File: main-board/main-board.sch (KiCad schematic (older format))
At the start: 57 parts, among them J1 C10418, J2 FH12-24S-0.5SH(55), J3 TF-01A, Q1 Q_NPN_BCE, Q2 Q_NPN_BCE, SW1 SW_DIP_x01, U1 ESP-32s, U2 HT7333-A, U3 CH340E, U4 DW06D, U5 IPS6404L-SQ-SPN, U6 SX1308, U7 RT9011-CMGJ6, U8 SN74LVC125ADBR

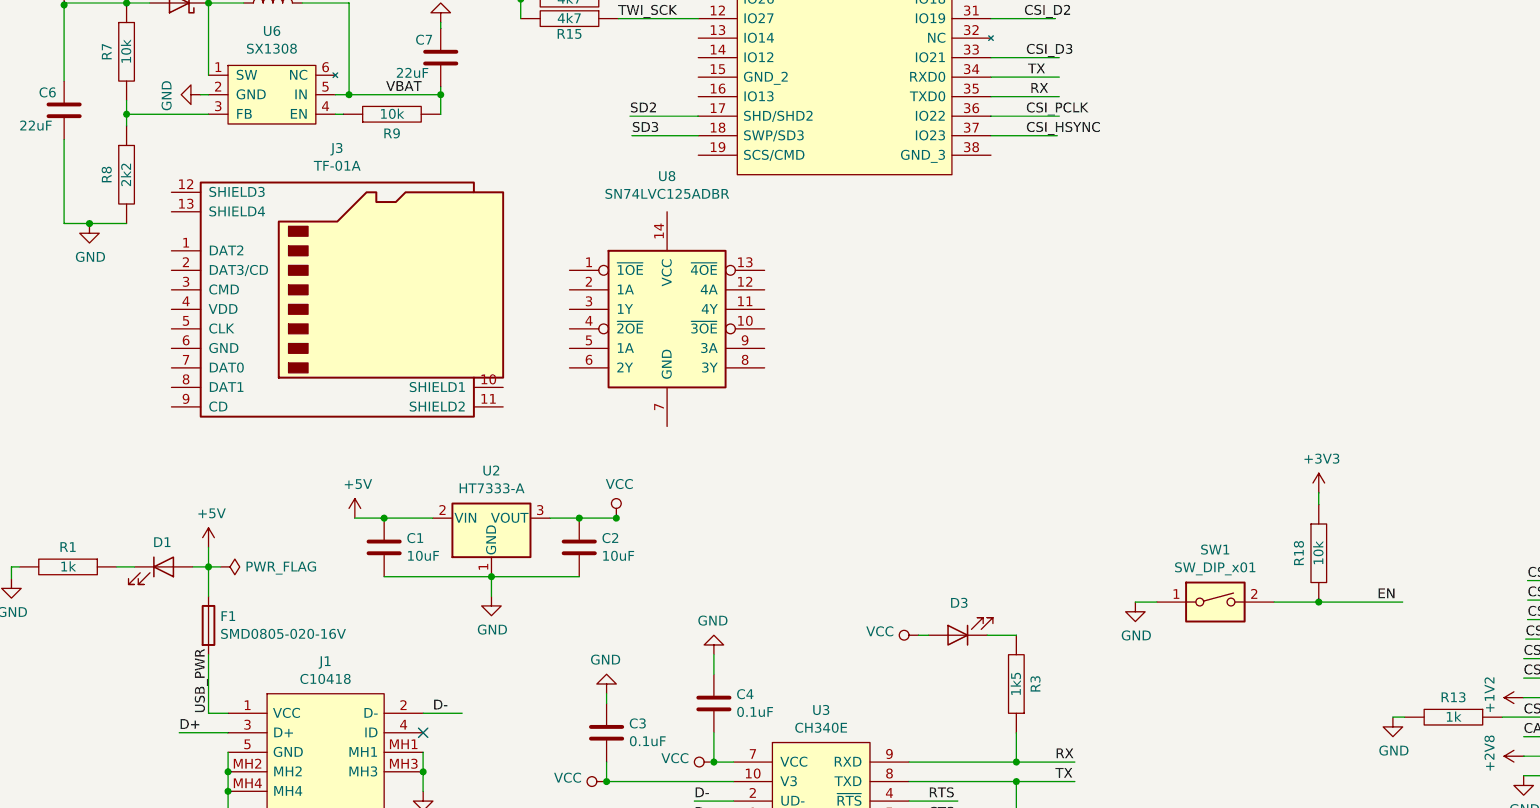
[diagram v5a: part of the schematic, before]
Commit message: SD passive and wires
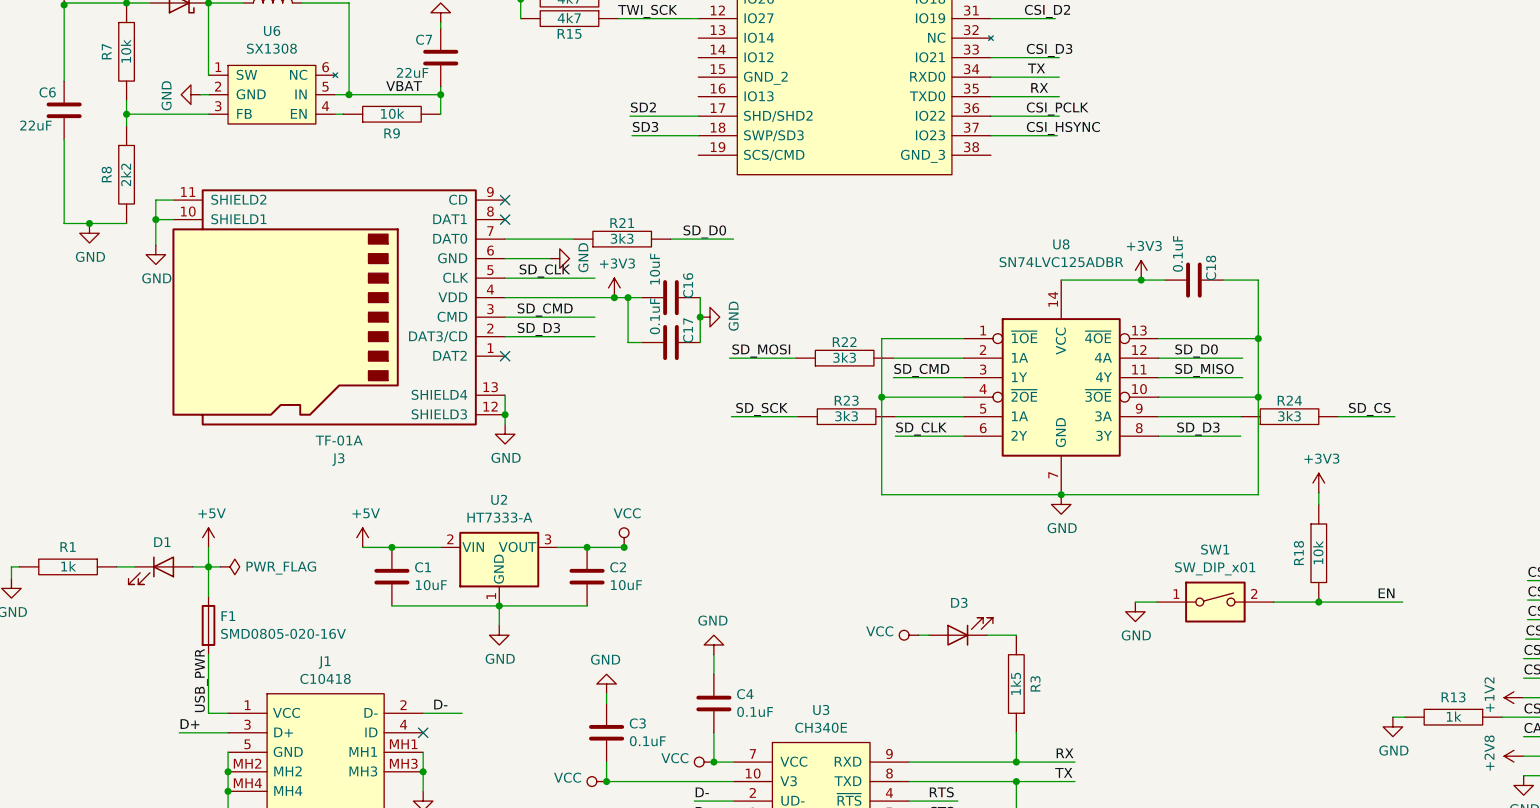
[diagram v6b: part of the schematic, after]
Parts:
- added C16: 10uF, Capacitor_SMD:C_0805_2012Metric_Pad1.15x1.40mm_HandSolder, symbol Device:C
- added C17, C18: 0.1uF, Capacitor_SMD:C_0805_2012Metric_Pad1.15x1.40mm_HandSolder, symbol Device:C
- added R21, R22, R23, R24: 3k3, Resistor_SMD:R_0805_2012Metric_Pad1.15x1.40mm_HandSolder, symbol pspice:R
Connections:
- net labels added: SD_CLK, SD_CMD, SD_CS, SD_D0, SD_D3, SD_MISO, SD_MOSI, SD_SCK
- wire segments 201 -> 245
- no-connect marks 5 -> 8
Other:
- moved on the sheet: C1, C2, J3, U2, U8

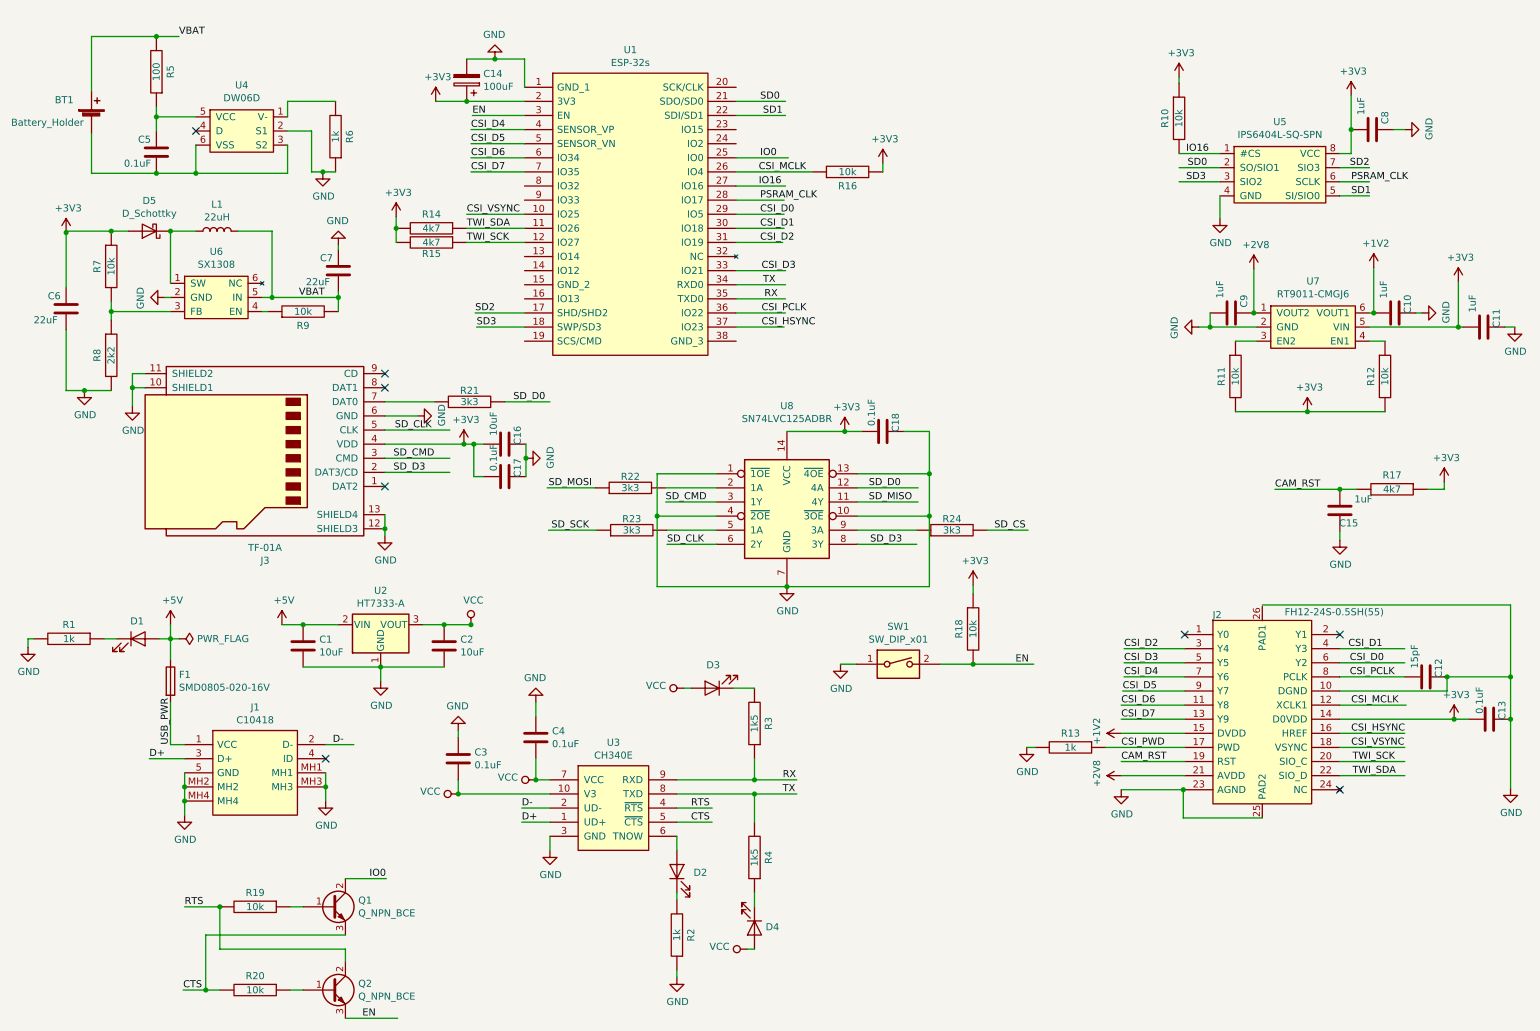
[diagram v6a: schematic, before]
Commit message: LED and few connection
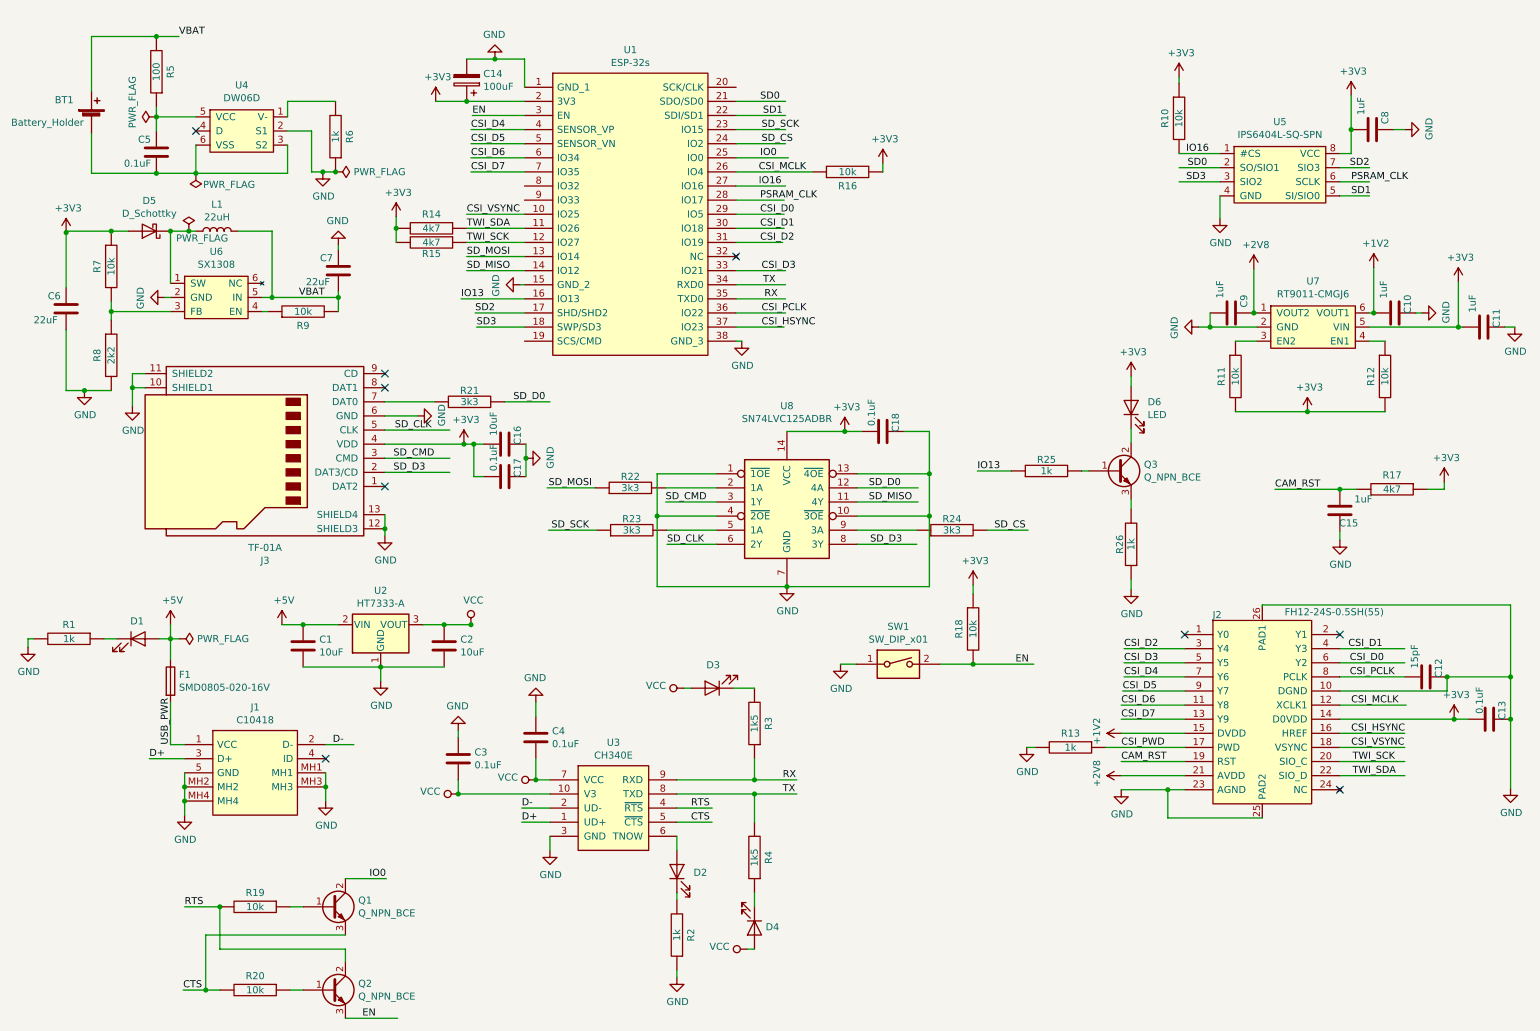
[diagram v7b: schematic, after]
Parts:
- added D6: LED, LED_THT:LED_D3.0mm, symbol Device:LED
- added Q3: Q_NPN_BCE, Package_TO_SOT_SMD:SOT-23, symbol Device:Q_NPN_BCE
- added R25, R26: 1k, Resistor_SMD:R_0805_2012Metric_Pad1.15x1.40mm_HandSolder, symbol pspice:R
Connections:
- net labels added: IO13
- wire segments 245 -> 260
- no-connect marks 8 -> 9
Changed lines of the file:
@@
 Text Label 5940 6050 0    50   ~ 0
 TX
-Wire Wire Line
-	1600 5400 1600 5700
 $Comp
 L power:PWR_FLAG #FLG0101
@@
 	2320 2530 2790 2530
 Wire Wire Line
-	1780 2060 1600 2060
+	1780 2060 1730 2060
 Wire Wire Line
 	1600 2060 1600 2430
@@
 Wire Wire Line
 	990  3190 1180 3190
-Wire Wire Line
-	860  2460 860  2070
 Wire Wire Line
 	860  2060 1180 2060
@@
 	8790 5920 8340 5920
 Wire Wire Line
-	8790 6020 8780 6020
+	8790 6020 8670 6020
 NoConn ~ 8790 4920
 NoConn ~ 9890 4920
@@
 $EndComp
 Wire Wire Line
-	9340 6220 8780 6220
-Wire Wire Line
-	8780 6220 8780 6020
-Connection ~ 8780 6020
-Wire Wire Line
-	8780 6020 8340 6020
+	9340 6220 8670 6220
+Wire Wire Line
+	8670 6220 8670 6020
+Connection ~ 8670 6020
+Wire Wire Line
+	8670 6020 8340 6020
 Wire Wire Line
 	9340 4710 11100 4710
@@
 Wire Wire Line
 	5050 4080 5050 4580
+$Comp
+L Device:Q_NPN_BCE Q3
+U 1 1 5D9D459B
+P 8310 3760
+F 0 "Q3" H 8501 3806 50  0000 L CNN
+F 1 "Q_NPN_BCE" H 8501 3715 50  0000 L CNN
+F 2 "Package_TO_SOT_SMD:SOT-23" H 8510 3860 50  0001 C CNN
+F 3 "https://datasheet.lcsc.com/szlcsc/Changjiang-Electronics-Tech-CJ-S8050_C2146.pdf" H 8310 3760 50  0001 C CNN
+F 4 "C2146" H 8310 3760 50  0001 C CNN "LCSC"
+	1    8310 3760
+	1    0    0    -1
+$EndComp
+NoConn ~ 5610 2240
+$Comp
+L power:GND #PWR052
+U 1 1 5D9E8C86
+P 5650 2840
+F 0 "#PWR052" H 5650 2590 50  0001 C CNN
+F 1 "GND" H 5655 2667 50  0000 C CNN
+F 2 "" H 5650 2840 50  0001 C CNN
+F 3 "" H 5650 2840 50  0001 C CNN
+	1    5650 2840
+	1    0    0    -1
+$EndComp
+Wire Wire Line
+	5610 2840 5650 2840
+$Comp
+L power:GND #PWR051
+U 1 1 5D9FCC82
+P 4080 2440
+F 0 "#PWR051" H 4080 2190 50  0001 C CNN
+F 1 "GND" H 4085 2267 50  0000 C CNN
+F 2 "" H 4080 2440 50  0001 C CNN
+F 3 "" H 4080 2440 50  0001 C CNN
+	1    4080 2440
+	0    1    1    0
+$EndComp
+Wire Wire Line
+	4080 2440 4110 2440
+Wire Wire Line
+	4110 2540 3660 2540
+Text Label 3660 2540 0    50   ~ 0
+IO13
+$Comp
+L pspice:R R25
+U 1 1 5DA399B3
+P 7810 3760
+F 0 "R25" V 7890 3760 50  0000 C CNN
+F 1 "1k" V 7810 3760 50  0000 C CNN
+F 2 "Resistor_SMD:R_0805_2012Metric_Pad1.15x1.40mm_HandSolder" H 7810 3760 50  0001 C CNN
+F 3 "~" H 7810 3760 50  0001 C CNN
+	1    7810 3760
+	0    -1   -1   0
+$EndComp
+Wire Wire Line
+	8060 3760 8110 3760
+Wire Wire Line
+	7560 3760 7320 3760
+Text Label 7320 3760 0    50   ~ 0
+IO13
+$Comp
+L Device:LED D6
+U 1 1 5DA76080
+P 8410 3310
+F 0 "D6" V 8449 3193 50  0000 R CNN
+F 1 "LED" V 8358 3193 50  0000 R CNN
+F 2 "LED_THT:LED_D3.0mm" H 8410 3310 50  0001 C CNN
+F 3 "https://datasheet.lcsc.com/szlcsc/Vishay-Intertech-TSAL6100_C111836.pdf" H 8410 3310 50  0001 C CNN
+F 4 "C111836" V 8410 3310 50  0001 C CNN "LCSC"
+	1    8410 3310
+	0    -1   -1   0
+$EndComp
+$Comp
+L pspice:R R26
+U 1 1 5DA790E1
+P 8410 4280
+F 0 "R26" V 8490 4280 50  0000 C CNN
+F 1 "1k" V 8410 4280 50  0000 C CNN
+F 2 "Resistor_SMD:R_0805_2012Metric_Pad1.15x1.40mm_HandSolder" H 8410 4280 50  0001 C CNN
+F 3 "~" H 8410 4280 50  0001 C CNN
+	1    8410 4280
+	-1   0    0    1
+$EndComp
+$Comp
+L power:GND #PWR054
+U 1 1 5DA7A289
+P 8410 4600
+F 0 "#PWR054" H 8410 4350 50  0001 C CNN
+F 1 "GND" H 8415 4427 50  0000 C CNN
+F 2 "" H 8410 4600 50  0001 C CNN
+F 3 "" H 8410 4600 50  0001 C CNN
+	1    8410 4600
+	1    0    0    -1
+$EndComp
+$Comp
+L power:+3V3 #PWR053
+U 1 1 5DA7CA61
+P 8410 3090
+F 0 "#PWR053" H 8410 2940 50  0001 C CNN
+F 1 "+3V3" H 8425 3263 50  0000 C CNN
+F 2 "" H 8410 3090 50  0001 C CNN
+F 3 "" H 8410 3090 50  0001 C CNN
+	1    8410 3090
+	1    0    0    -1
+$EndComp
+Wire Wire Line
+	8410 3090 8410 3160
+Wire Wire Line
+	8410 3460 8410 3560
+Wire Wire Line
+	8410 3960 8410 4030
+Wire Wire Line
+	8410 4530 8410 4600
+$Comp
+L power:PWR_FLAG #FLG0102
+U 1 1 5DB11B0F
+P 2770 1640
+F 0 "#FLG0102" H 2770 1715 50  0001 C CNN
+F 1 "PWR_FLAG" V 2770 1768 50  0000 L CNN
+F 2 "" H 2770 1640 50  0001 C CNN
+F 3 "~" H 2770 1640 50  0001 C CNN
+	1    2770 1640
+	0    1    1    0
+$EndComp
+Connection ~ 2770 1640
+Wire Wire Line
+	1600 5400 1600 5700
+$Comp
+L power:PWR_FLAG #FLG0103
+U 1 1 5DBB358B
+P 1500 1250
+F 0 "#FLG0103" H 1500 1325 50  0001 C CNN
+F 1 "PWR_FLAG" H 1420 1420 50  0000 L CNN
+F 2 "" H 1500 1250 50  0001 C CNN
+F 3 "~" H 1500 1250 50  0001 C CNN
+	1    1500 1250
+	0    -1   -1   0
+$EndComp
+$Comp
+L power:PWR_FLAG #FLG0104
+U 1 1 5DBB6BA6
+P 1780 1650
+F 0 "#FLG0104" H 1780 1725 50  0001 C CNN
+F 1 "PWR_FLAG" H 1360 1730 50  0000 L CNN
+F 2 "" H 1780 1650 50  0001 C CNN
+F 3 "~" H 1780 1650 50  0001 C CNN
+	1    1780 1650
+	-1   0    0    1
+$EndComp
+$Comp
+L power:PWR_FLAG #FLG0105
+U 1 1 5DBB9B47
+P 1730 2060
+F 0 "#FLG0105" H 1730 2135 50  0001 C CNN
+F 1 "PWR_FLAG" H 1640 2010 50  0000 L CNN
+F 2 "" H 1730 2060 50  0001 C CNN
+F 3 "~" H 1730 2060 50  0001 C CNN
+	1    1730 2060
+	1    0    0    -1
+$EndComp
+Connection ~ 1730 2060
+Wire Wire Line
+	1730 2060 1600 2060
+Wire Wire Line
+	9340 4710 9340 4720
+Wire Wire Line
+	860  2070 860  2460
+Wire Wire Line
+	4110 2240 3700 2240
+Text Label 3700 2240 0    50   ~ 0
+SD_MOSI
+Wire Wire Line
+	4110 2340 3700 2340
+Text Label 3700 2340 0    50   ~ 0
+SD_MISO
+Text Label 5790 1340 0    50   ~ 0
+SD_SCK
+Text Label 5790 1440 0    50   ~ 0
+SD_CS
+Wire Wire Line
+	5610 1340 5960 1340
+Wire Wire Line
+	5610 1440 5960 1440
 $EndSCHEMATC

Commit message: LED SMD
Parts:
- removed D6: LED, LED_THT:LED_D3.0mm, symbol Device:LED
- added C19: 1uF, Capacitor_SMD:C_0805_2012Metric_Pad1.15x1.40mm_HandSolder, symbol Device:C
- added D6: HQ67-2100IRC, water-lib:HQ67-2100IRC, symbol water-lib:HQ67-2100IRC
- added Q4: DMG1012T, water-lib:SOT-523, symbol Device:Q_NMOS_GDS
- added R27: 27k, Resistor_SMD:R_0805_2012Metric_Pad1.15x1.40mm_HandSolder, symbol pspice:R
- added R28: 10k, Resistor_SMD:R_0805_2012Metric_Pad1.15x1.40mm_HandSolder, symbol pspice:R
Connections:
- net labels added: BAT_ST, IO32
- wire segments 260 -> 272
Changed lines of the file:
@@
 IO13
-$Comp
-L Device:LED D6
-U 1 1 5DA76080
-P 8410 3310
-F 0 "D6" V 8449 3193 50  0000 R CNN
-F 1 "LED" V 8358 3193 50  0000 R CNN
-F 2 "LED_THT:LED_D3.0mm" H 8410 3310 50  0001 C CNN
-F 3 "https://datasheet.lcsc.com/szlcsc/Vishay-Intertech-TSAL6100_C111836.pdf" H 8410 3310 50  0001 C CNN
-F 4 "C111836" V 8410 3310 50  0001 C CNN "LCSC"
-	1    8410 3310
-	0    -1   -1   0
-$EndComp
 $Comp
 L pspice:R R26
@@
 Wire Wire Line
 	5610 1440 5960 1440
+$Comp
+L Device:Q_NMOS_GDS Q4
+U 1 1 5DC5DFE6
+P 7670 2050
+F 0 "Q4" H 7876 2096 50  0000 L CNN
+F 1 "DMG1012T" H 7876 2005 50  0000 L CNN
+F 2 "water-lib:SOT-523" H 7870 2150 50  0001 C CNN
+F 3 "https://datasheet.lcsc.com/szlcsc/Diodes-Incorporated-DMG1012T-7_C20512.pdf" H 7670 2050 50  0001 C CNN
+F 4 "C20512" H 7670 2050 50  0001 C CNN "LCSC"
+	1    7670 2050
+	1    0    0    -1
+$EndComp
+$Comp
+L pspice:R R27
+U 1 1 5DC622A1
+P 7770 1560
+F 0 "R27" V 7670 1560 50  0000 C CNN
+F 1 "27k" V 7770 1560 50  0000 C CNN
+F 2 "Resistor_SMD:R_0805_2012Metric_Pad1.15x1.40mm_HandSolder" H 7770 1560 50  0001 C CNN
+F 3 "~" H 7770 1560 50  0001 C CNN
+	1    7770 1560
+	1    0    0    -1
+$EndComp
+Wire Wire Line
+	7770 1310 7770 1060
+Wire Wire Line
+	7770 1810 7770 1850
+Text Label 7770 1240 1    50   ~ 0
+VBAT
+Wire Wire Line
+	7470 2050 7170 2050
+Wire Wire Line
+	4110 1840 3710 1840
+Text Label 3710 1840 0    50   ~ 0
+BAT_ST
+Text Label 7170 2050 0    50   ~ 0
+BAT_ST
+Wire Wire Line
+	4110 1740 3720 1740
+Text Label 3720 1740 0    50   ~ 0
+IO32
+Text Label 8160 2280 0    50   ~ 0
+IO32
+$Comp
+L pspice:R R28
+U 1 1 5DCE7D22
+P 7770 2530
+F 0 "R28" V 7670 2530 50  0000 C CNN
+F 1 "10k" V 7770 2530 50  0000 C CNN
+F 2 "Resistor_SMD:R_0805_2012Metric_Pad1.15x1.40mm_HandSolder" H 7770 2530 50  0001 C CNN
+F 3 "~" H 7770 2530 50  0001 C CNN
+	1    7770 2530
+	1    0    0    -1
+$EndComp
+$Comp
+L power:GND #PWR055
+U 1 1 5DCE8734
+P 7770 2820
+F 0 "#PWR055" H 7770 2570 50  0001 C CNN
+F 1 "GND" H 7775 2647 50  0000 C CNN
+F 2 "" H 7770 2820 50  0001 C CNN
+F 3 "" H 7770 2820 50  0001 C CNN
+	1    7770 2820
+	1    0    0    -1
+$EndComp
+$Comp
+L Device:C C19
+U 1 1 5DCE9114
+P 8060 2540
+F 0 "C19" H 7930 2630 50  0000 L CNN
+F 1 "1uF" H 7830 2460 50  0000 L CNN
+F 2 "Capacitor_SMD:C_0805_2012Metric_Pad1.15x1.40mm_HandSolder" H 8098 2390 50  0001 C CNN
+F 3 "~" H 8060 2540 50  0001 C CNN
+	1    8060 2540
+	-1   0    0    1
+$EndComp
+Wire Wire Line
+	7770 2250 7770 2280
+Wire Wire Line
+	7770 2780 7770 2820
+Wire Wire Line
+	7770 2280 8060 2280
+Wire Wire Line
+	8060 2280 8060 2390
+Connection ~ 7770 2280
+Wire Wire Line
+	8060 2690 8060 2780
+Wire Wire Line
+	8060 2780 7770 2780
+Connection ~ 7770 2780
+Wire Wire Line
+	8060 2280 8330 2280
+Connection ~ 8060 2280
+$Comp
+L water-lib:HQ67-2100IRC D6
+U 1 1 5DD8FA79
+P 8410 3310
+F 0 "D6" V 8449 3193 50  0000 R CNN
+F 1 "HQ67-2100IRC" V 8358 3193 50  0000 R CNN
+F 2 "water-lib:HQ67-2100IRC" H 8410 2960 50  0001 C CNN
+F 3 "https://datasheet.lcsc.com/szlcsc/HARVATEK-HQ67-2100IRC_C258876.pdf" H 8410 3310 50  0001 C CNN
+F 4 "C258876" H 8410 3060 50  0001 C CNN "LCSC"
+	1    8410 3310
+	0    -1   -1   0
+$EndComp
 $EndSCHEMATC
